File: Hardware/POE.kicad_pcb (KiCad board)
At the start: 2 copper layers, 34 x 34 mm, 20 parts, among them J10 Conn_01x02_Male, J11 Conn_01x02_Male, J3 Conn_01x02_Male, J4 Conn_01x02_Male, J5 Conn_01x02_Male, J6 Conn_01x02_Male, J7 Conn_01x08_Male, J9 QWIIC_Stackable

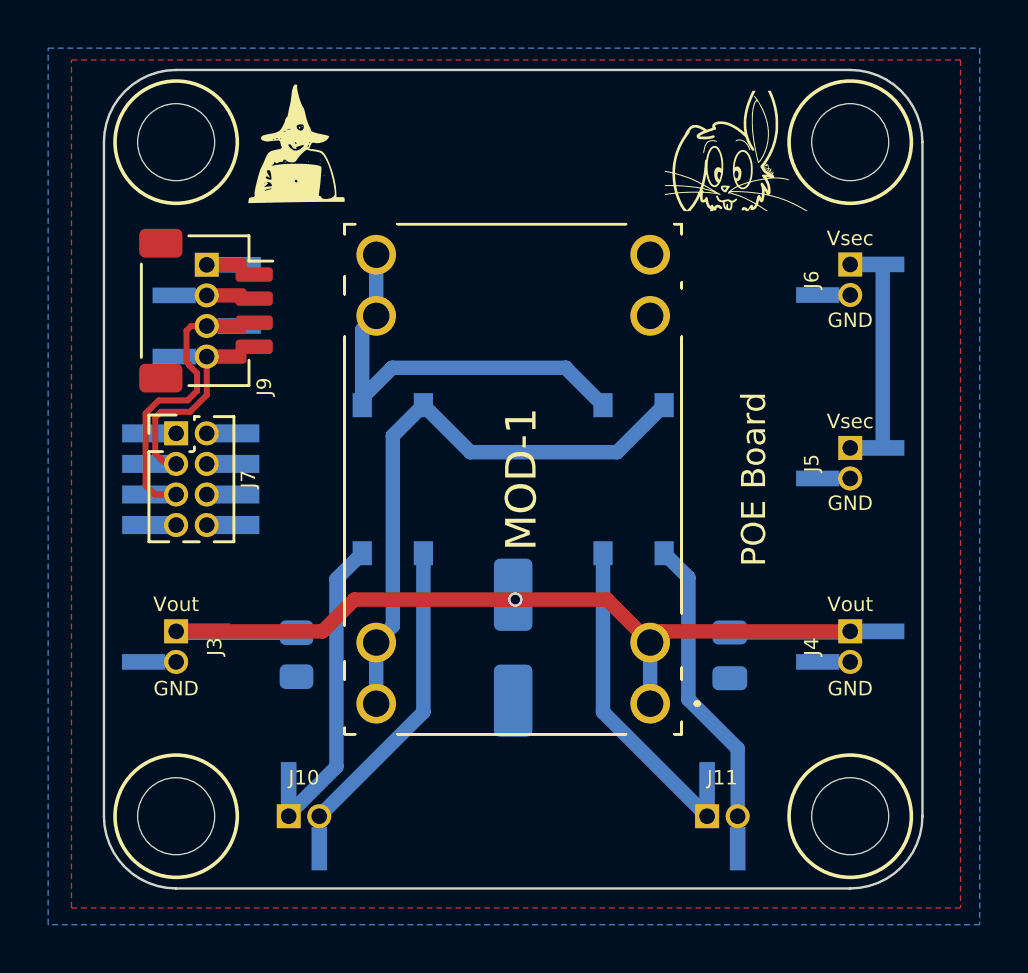
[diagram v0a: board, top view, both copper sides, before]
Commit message: Updated POE Board for J7/J9
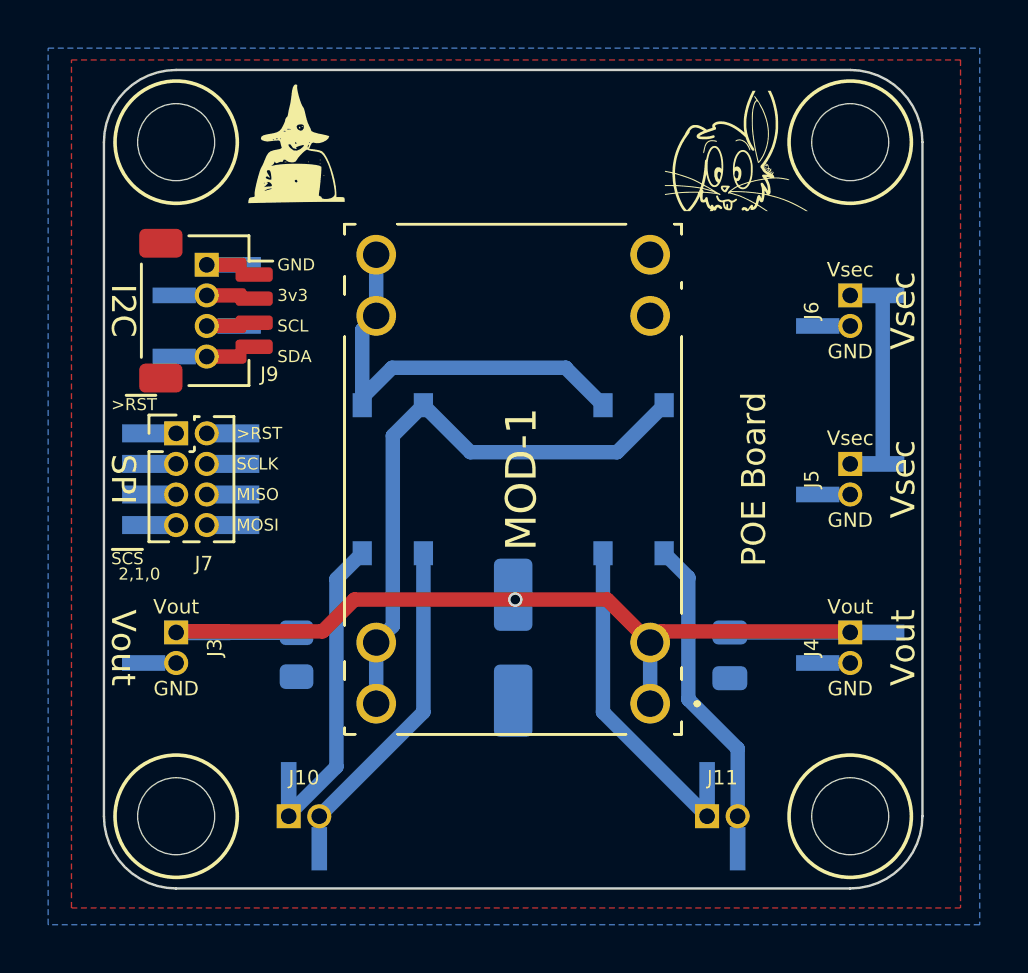
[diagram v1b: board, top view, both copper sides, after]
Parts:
- moved J6 1.28 mm to (114.0, 92.4)
- moved J5 0.66 mm to (114.0, 99.4)
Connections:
- net WIZ_RST renamed ~{RESET}
- J7 pad 2: SCLK -> RESET
- J7 pad 3: SCL -> ~{SCS}2
- J7 pad 4: MISO -> SCLK
- J7 pad 5: SDA -> ~{SCS}1
- J7 pad 6: MOSI -> MISO
- J7 pad 7: unconnected-(J7-Pad7) -> ~{SCS}0
- J7 pad 8: ~{SCS} -> MOSI
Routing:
- net SDA: track 10.6 -> 0.00 mm
- net SCL: track 6.15 -> 0.00 mm
- net Vsec: track 8.97 -> 7.00 mm
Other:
- board text added: "2,1,0"
- board text added: "3v3"
- board text added: ">RST"
- board text added: ">~{RST}"
- board text added: "MISO"
- board text added: "MOSI"
- board text added: "SCL"
- board text added: "SCLK"
- board text added: "SDA"
- board text added: "SPI"
- board text added: "~{SCS}"
